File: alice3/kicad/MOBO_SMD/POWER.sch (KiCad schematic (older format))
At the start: 3 parts, among them U8 LD29080DT33R

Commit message: Fix some footprint assignments.
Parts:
- C19, C20: footprint Capacitors_ThroughHole:C_Radial_D5_L11_P2.5 -> Capacitors_SMD:C_1206
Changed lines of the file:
@@
 $EndComp
 $Comp
-L GND #PWR051
+L GND #PWR052
 U 1 1 56BA78E3
 P 7300 2200
-F 0 "#PWR051" H 7300 1950 50  0001 C CNN
+F 0 "#PWR052" H 7300 1950 50  0001 C CNN
 F 1 "GND" H 7300 2050 50  0000 C CNN
 F 2 "" H 7300 2200 60  0000 C CNN
@@
 F 0 "C19" H 6810 1970 50  0000 L CNN
 F 1 "10µF" H 6810 1820 50  0000 L CNN
-F 2 "Capacitors_ThroughHole:C_Radial_D5_L11_P2.5" H 6800 1900 60  0001 C CNN
+F 2 "Capacitors_SMD:C_1206" H 6800 1900 60  0001 C CNN
 F 3 "" H 6800 1900 60  0000 C CNN
 	1    6800 1900
@@
 F 0 "C20" H 7810 1970 50  0000 L CNN
 F 1 "10µF" H 7810 1820 50  0000 L CNN
-F 2 "Capacitors_ThroughHole:C_Radial_D5_L11_P2.5" H 7800 1900 60  0001 C CNN
+F 2 "Capacitors_SMD:C_1206" H 7800 1900 60  0001 C CNN
 F 3 "" H 7800 1900 60  0000 C CNN
 	1    7800 1900
@@
 	7800 2100 7800 2000
 $Comp
-L +3V3 #PWR052
+L +3V3 #PWR053
 U 1 1 56BA7A57
 P 7800 1300
-F 0 "#PWR052" H 7800 1150 50  0001 C CNN
+F 0 "#PWR053" H 7800 1150 50  0001 C CNN
 F 1 "+3V3" H 7800 1440 50  0000 C CNN
 F 2 "" H 7800 1300 60  0000 C CNN
@@
 Connection ~ 7800 1600
 $Comp
-L +5V #PWR053
+L +5V #PWR054
 U 1 1 56BA7A9A
 P 6800 1300
-F 0 "#PWR053" H 6800 1150 50  0001 C CNN
+F 0 "#PWR054" H 6800 1150 50  0001 C CNN
 F 1 "+5V" H 6800 1440 50  0000 C CNN
 F 2 "" H 6800 1300 60  0000 C CNN

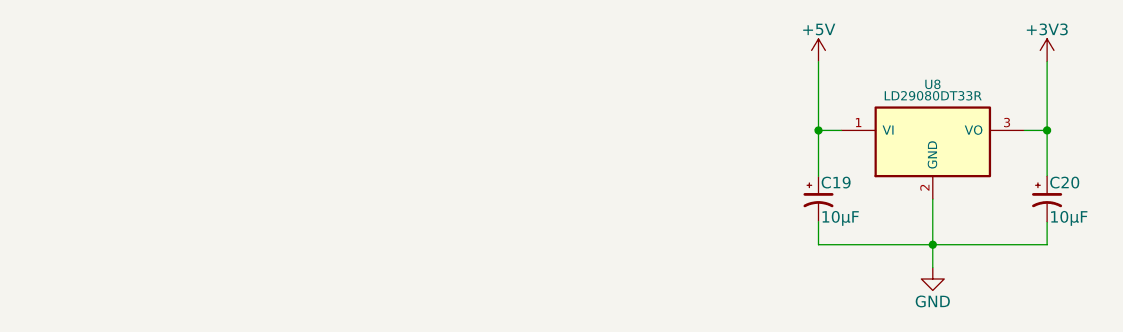
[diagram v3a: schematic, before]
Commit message: 1st set MOBO schematic fixes for 1st PCBWay spin
Various fixes for KiCAD messing up components

Button on BOOT0

No huge cap on power supply LED

Discard RAM

Route ARM to Z80 /WAIT and /RFSH

Use "~" for active-low lines (shown in schematic by line above them)
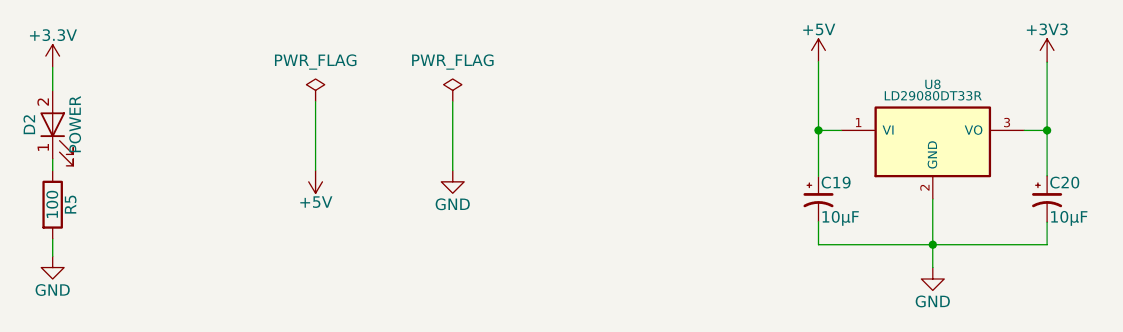
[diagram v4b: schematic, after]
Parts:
- added D2: POWER, LEDs:LED_0805, symbol LED
- added R5: 100, Resistors_SMD:R_0805, symbol R
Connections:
- net +3V3: now also D2.2 (A)
- net GND: now also R5.2
- new net: D2.1 (K), R5.1
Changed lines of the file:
@@
 $EndComp
 $Comp
-L GND #PWR051
+L GND #PWR042
 U 1 1 56BA78E3
 P 7300 2200
-F 0 "#PWR051" H 7300 1950 50  0001 C CNN
+F 0 "#PWR042" H 7300 1950 50  0001 C CNN
 F 1 "GND" H 7300 2050 50  0000 C CNN
 F 2 "" H 7300 2200 60  0000 C CNN
@@
 	7800 2100 7800 2000
 $Comp
-L +3V3 #PWR052
+L +3V3 #PWR043
 U 1 1 56BA7A57
 P 7800 1300
-F 0 "#PWR052" H 7800 1150 50  0001 C CNN
+F 0 "#PWR043" H 7800 1150 50  0001 C CNN
 F 1 "+3V3" H 7800 1440 50  0000 C CNN
 F 2 "" H 7800 1300 60  0000 C CNN
@@
 Connection ~ 7800 1600
 $Comp
-L +5V #PWR053
+L +5V #PWR044
 U 1 1 56BA7A9A
 P 6800 1300
-F 0 "#PWR053" H 6800 1150 50  0001 C CNN
+F 0 "#PWR044" H 6800 1150 50  0001 C CNN
 F 1 "+5V" H 6800 1440 50  0000 C CNN
 F 2 "" H 6800 1300 60  0000 C CNN
@@
 $EndComp
 Connection ~ 6800 1600
+$Comp
+L PWR_FLAG #FLG045
+U 1 1 59A49B7F
+P 4600 1475
+F 0 "#FLG045" H 4600 1570 50  0001 C CNN
+F 1 "PWR_FLAG" H 4600 1655 50  0000 C CNN
+F 2 "" H 4600 1475 50  0000 C CNN
+F 3 "" H 4600 1475 50  0000 C CNN
+	1    4600 1475
+	1    0    0    -1
+$EndComp
+$Comp
+L +5V #PWR046
+U 1 1 59A49B85
+P 4600 1775
+F 0 "#PWR046" H 4600 1625 50  0001 C CNN
+F 1 "+5V" H 4600 1915 50  0000 C CNN
+F 2 "" H 4600 1775 50  0000 C CNN
+F 3 "" H 4600 1775 50  0000 C CNN
+	1    4600 1775
+	-1   0    0    1
+$EndComp
+$Comp
+L PWR_FLAG #FLG047
+U 1 1 59A49B8B
+P 5200 1475
+F 0 "#FLG047" H 5200 1570 50  0001 C CNN
+F 1 "PWR_FLAG" H 5200 1655 50  0000 C CNN
+F 2 "" H 5200 1475 50  0000 C CNN
+F 3 "" H 5200 1475 50  0000 C CNN
+	1    5200 1475
+	1    0    0    -1
+$EndComp
+$Comp
+L GND #PWR048
+U 1 1 59A49B91
+P 5200 1775
+F 0 "#PWR048" H 5200 1525 50  0001 C CNN
+F 1 "GND" H 5200 1625 50  0000 C CNN
+F 2 "" H 5200 1775 50  0000 C CNN
+F 3 "" H 5200 1775 50  0000 C CNN
+	1    5200 1775
+	1    0    0    -1
+$EndComp
+$Comp
+L GND #PWR049
+U 1 1 59A49B97
+P 3450 2150
+F 0 "#PWR049" H 3450 1900 50  0001 C CNN
+F 1 "GND" H 3450 2000 50  0000 C CNN
+F 2 "" H 3450 2150 50  0000 C CNN
+F 3 "" H 3450 2150 50  0000 C CNN
+	1    3450 2150
+	1    0    0    -1
+$EndComp
+$Comp
+L +3.3V #PWR050
+U 1 1 59A49B9D
+P 3450 1325
+F 0 "#PWR050" H 3450 1175 50  0001 C CNN
+F 1 "+3.3V" H 3450 1465 50  0000 C CNN
+F 2 "" H 3450 1325 50  0000 C CNN
+F 3 "" H 3450 1325 50  0000 C CNN
+	1    3450 1325
+	1    0    0    -1
+$EndComp
+$Comp
+L LED D2
+U 1 1 59A49BA3
+P 3450 1575
+F 0 "D2" H 3450 1675 50  0000 C CNN
+F 1 "POWER" H 3450 1475 50  0000 C CNN
+F 2 "LEDs:LED_0805" H 3450 1575 50  0001 C CNN
+F 3 "" H 3450 1575 50  0000 C CNN
+	1    3450 1575
+	0    -1   -1   0
+$EndComp
+$Comp
+L R R5
+U 1 1 59A49BAA
+P 3450 1925
+F 0 "R5" V 3530 1925 50  0000 C CNN
+F 1 "100" V 3450 1925 50  0000 C CNN
+F 2 "Resistors_SMD:R_0805" V 3380 1925 50  0001 C CNN
+F 3 "" H 3450 1925 50  0000 C CNN
+	1    3450 1925
+	1    0    0    -1
+$EndComp
+Wire Wire Line
+	4600 1475 4600 1775
+Wire Wire Line
+	5200 1775 5200 1475
+Wire Wire Line
+	3450 1725 3450 1775
+Wire Wire Line
+	3450 2075 3450 2150
+Wire Wire Line
+	3450 1325 3450 1425
 $EndSCHEMATC

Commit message: fix inductor, fix HOME
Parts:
- U8: Distributor (none) -> Digikey; Distributor PN (none) -> 497-13047-1-ND; Manufacturer (none) -> STMicroelectronics; PN (none) -> LD29080S33R
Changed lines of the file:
@@
 LIBS:propeller_p8x32a-q44
 LIBS:as6c2008_tsop
+LIBS:conn-fci
 LIBS:MOBO_SMD-cache
 EELAYER 25 0
@@
 F 2 "TO_SOT_Packages_SMD:SOT-223" H 7300 1750 40  0001 C CNN
 F 3 "" H 7300 1650 60  0000 C CNN
+F 4 "STMicroelectronics" H 975 3575 60  0001 C CNN "Manufacturer"
+F 5 "LD29080S33R" H 975 3575 60  0001 C CNN "PN"
+F 6 "Digikey" H 975 3575 60  0001 C CNN "Distributor"
+F 7 "497-13047-1-ND" H 975 3575 60  0001 C CNN "Distributor PN"
 	1    7300 1650
 	1    0    0    -1
